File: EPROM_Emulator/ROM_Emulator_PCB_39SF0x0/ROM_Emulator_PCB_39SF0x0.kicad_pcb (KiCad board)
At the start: 2 copper layers, 21.6 x 62.2 mm, 10 parts, among them U1 SST39SF040, U2 Teensy4.1_Fewer_Pins, U3 74HC244, U4 74HC244, U5 74HC244, U7 74HC244

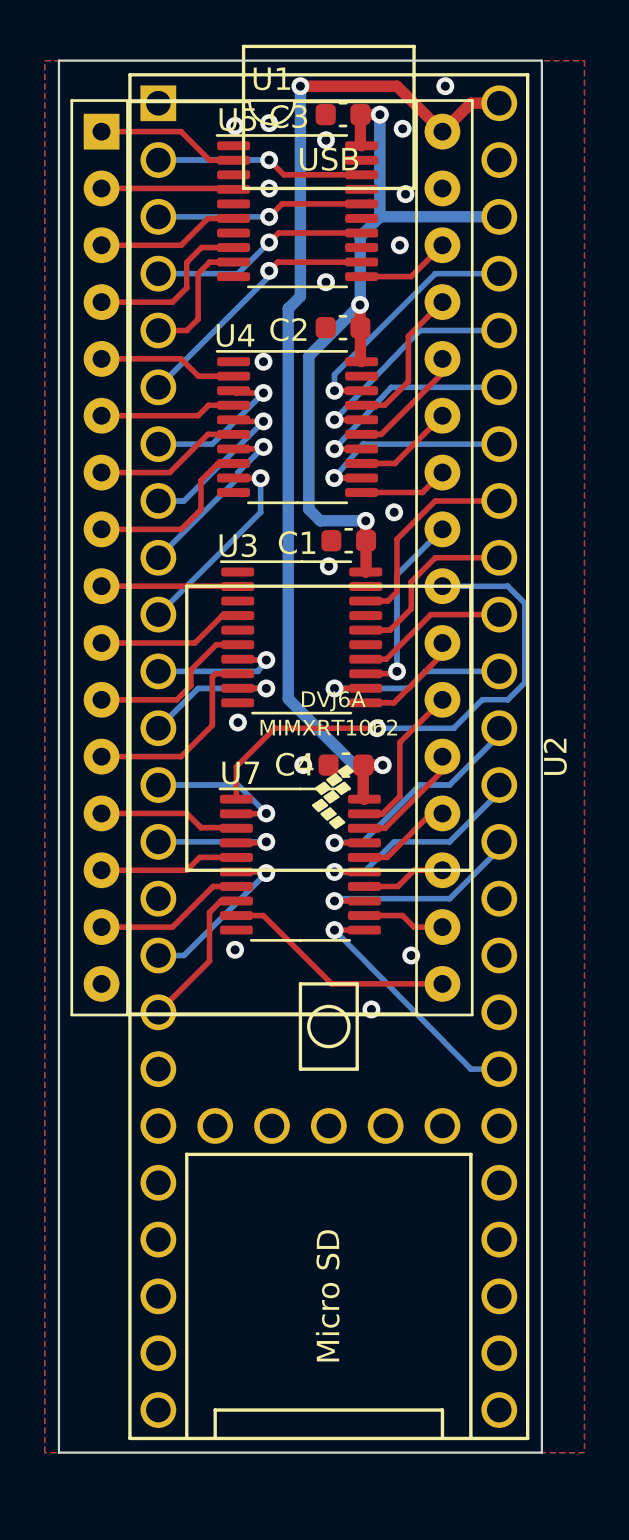
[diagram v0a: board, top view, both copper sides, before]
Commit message: Bugfix: OR'd OE# and CE# together, used for both halves of data 244. Added some buttons. Freed up D13 for LED use.
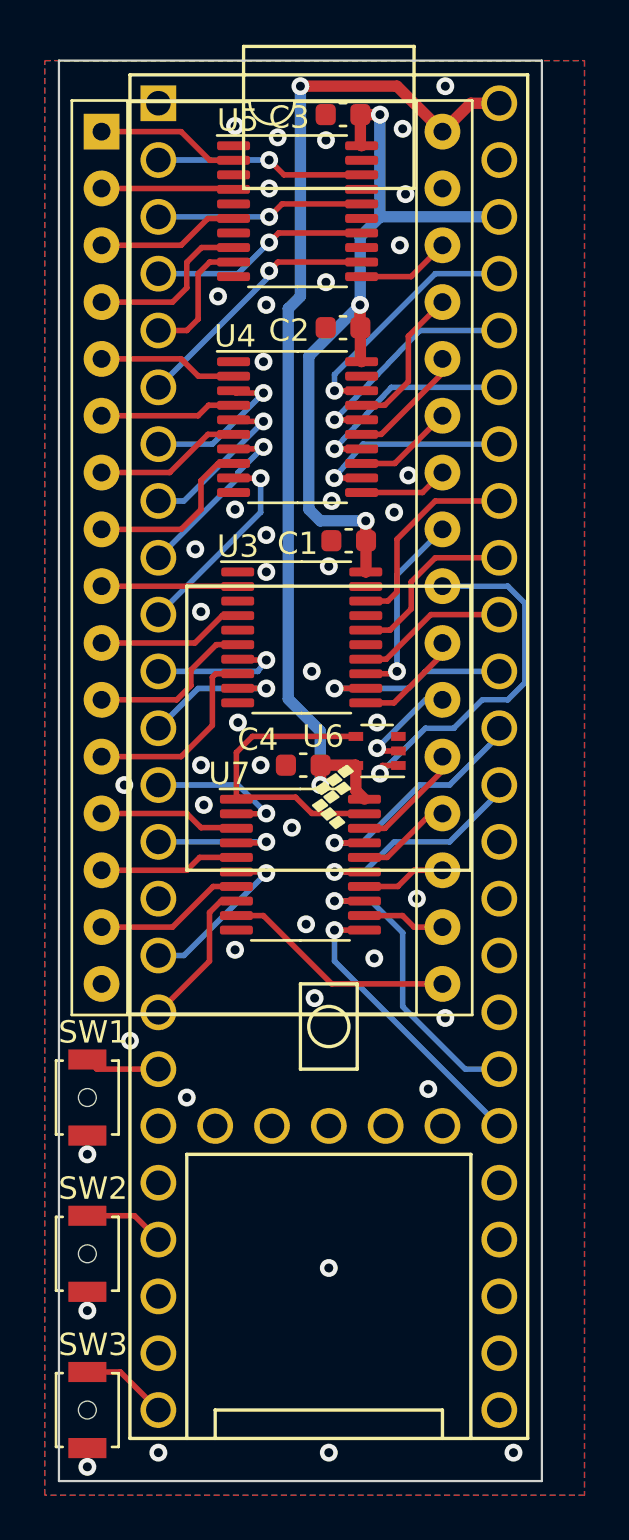
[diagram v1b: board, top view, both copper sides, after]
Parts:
- added SW1: SW_SPST, Button_Switch_SMD:SW_SPST_B3U-1000P-B, F.Cu at (125.1, 123.2)
- added SW2: SW_SPST, Button_Switch_SMD:SW_SPST_B3U-1000P-B, F.Cu at (125.1, 130.2)
- added SW3: SW_SPST, Button_Switch_SMD:SW_SPST_B3U-1000P-B, F.Cu at (125.1, 137.2)
- added U6: 74AHC1G32, Package_TO_SOT_SMD:SOT-353_SC-70-5, F.Cu at (138.0, 107.7)
- moved C4 1.90 mm to (134.7, 108.3)
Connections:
- U2 pad 18: unconnected-(U2-26_A12_MOSI1-Pad18) -> Net-(SW1-B)
- U2 pad 21: unconnected-(U2-29_TX7-Pad21) -> Net-(SW2-B)
- U2 pad 24: unconnected-(U2-32_OUT1B-Pad24) -> Net-(SW3-B)
- U2 pad 30: unconnected-(U2-38_CS1_IN1-Pad30) -> V3_D3
- U2 pad 31: V3_D3 -> V3_D2
- U2 pad 35: V3_D2 -> unconnected-(U2-13_SCK_LED-Pad35)
- U7 pad 1: ~{OE} -> Net-(U7-1OE)
- U7 pad 19: ~{CE} -> Net-(U7-1OE)
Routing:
- net Net-(U7-1OE): track 0.00 -> 13.8 mm
- net ~{OE}: track 23.5 -> 16.8 mm
- net Net-(SW3-B): track 0.00 -> 3.88 mm
- net V3_D2: track 10.3 -> 14.1 mm
- net Net-(SW2-B): track 0.00 -> 3.62 mm
- net Net-(SW1-B): track 0.00 -> 3.35 mm
- net ~{CE}: track 7.01 -> 4.80 mm, vias 0 -> 1
- net V3_D3: track 11.6 -> 13.4 mm
- net +5V: track 45.8 -> 46.5 mm
- net GND: vias 17 -> 45
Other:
- board size 21.6 x 62.2 mm -> 21.6 x 63.5 mm
- board text added: "39SF0x0 FLASH/PROM Emulator v1.0b 2023 @smitty@halibut.com Based on MicroCore Labs design"
- board text added: "<><"
- board text added: "><>"
- board text added: "O"
- board text added: "o"
